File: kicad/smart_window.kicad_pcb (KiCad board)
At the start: 2 copper layers, 88 x 71.5 mm, 84 parts, among them J1 PROG, J10 LS2, J11 Vin, J12 LS3, J13 Vmot1, J14 Vmot3, J2 Vmot2, J3 DOOR1, J4 MOT2, J5 MOT1, J6 MOT3, J7 I2C, J8 DOOR2, J9 LS1, Q10 BC807-40_215, Q11 BC817-40_215, Q12 BC807-40_215, Q13 BC817-40_215, Q15 BC817-40_215, Q17 BC807-40_215, Q18 BC817-40_215, Q19 BC807-40_215, Q20 BC817-40_215, Q22 BC817-40_215, Q24 BC807-40_215, Q25 BC817-40_215, Q26 BC807-40_215, Q27 BC817-40_215, Q4 BC817-40_215, U1 ESP-12F, U3 LTV-817S, U4 LTV-817S, U5 LTV-817S, U6 LTV-817S, U7 LTV-817S, U8 LTV-817S

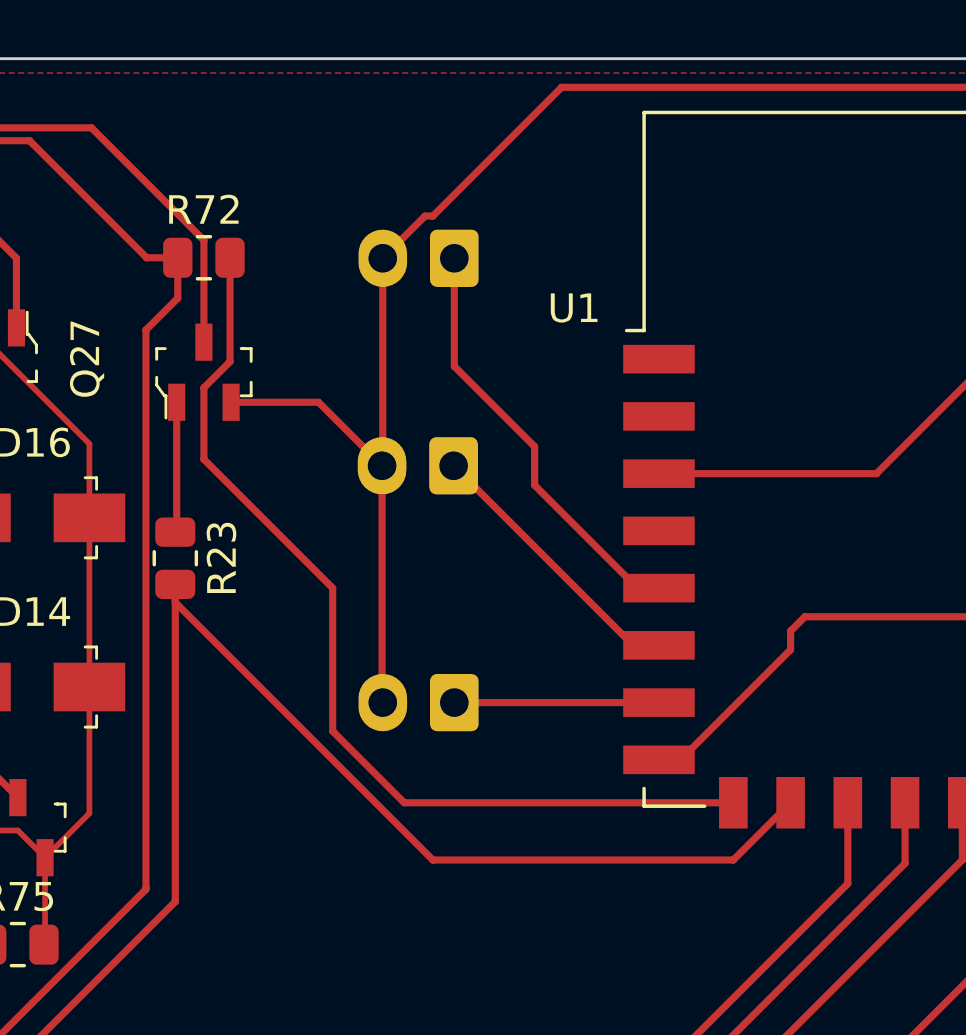
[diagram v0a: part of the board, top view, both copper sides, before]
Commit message: добавил фотосенсор
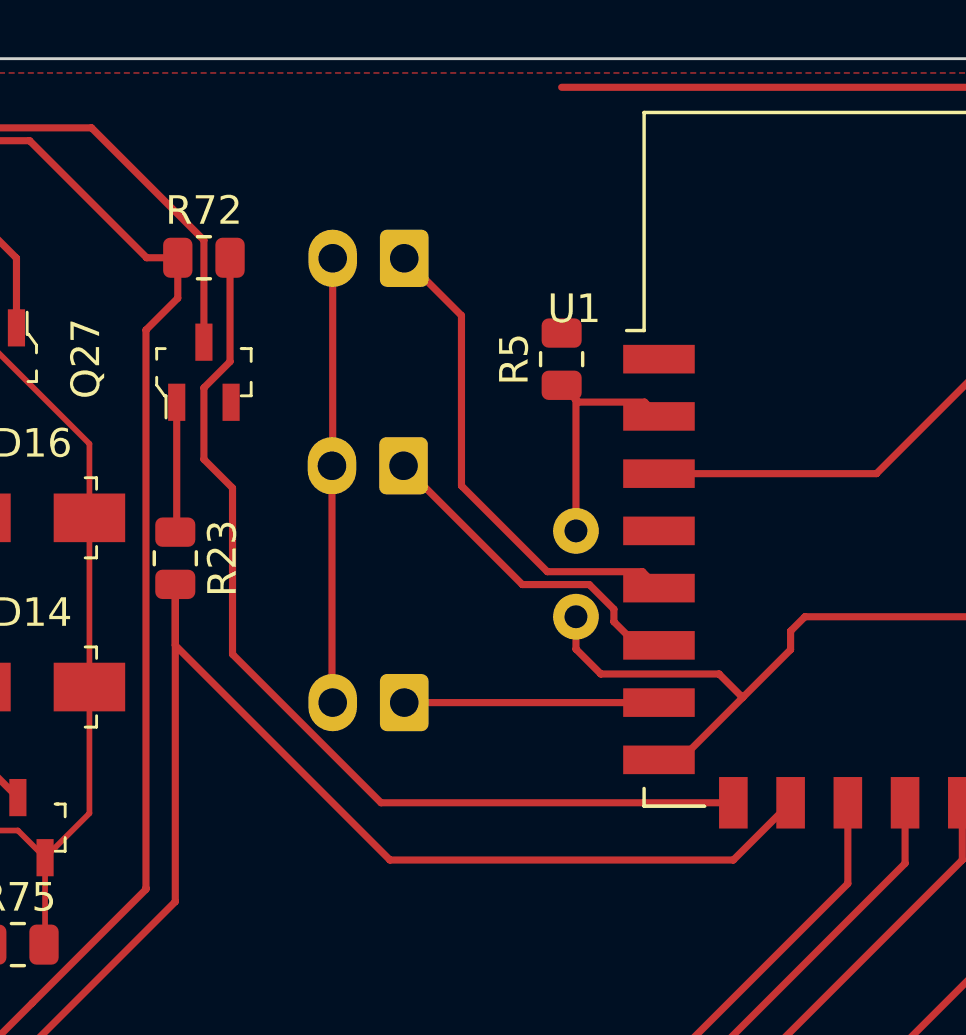
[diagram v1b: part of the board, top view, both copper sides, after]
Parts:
- added R4: A9050, OptoDevice:R_LDR_5.0x4.1mm_P3mm_Vertical, B.Cu at (131.5, 36.5)
- added R5: 500, Resistor_SMD:R_0805_2012Metric, F.Cu at (131.0, 27.5)
- moved J12 1.75 mm to (125.5, 39.5)
- moved J3 1.75 mm to (125.5, 24.0)
- moved J8 1.75 mm to (125.5, 31.2)
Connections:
- U1 pad 2: unconnected-(U1-Pad2) -> /LDR
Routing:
- net GND: track 240.0 -> 225.1 mm
- net /LDR: track 0.00 -> 9.15 mm
- net +3V3: track 41.3 -> 48.9 mm
- net /DOOR1: track 14.9 -> 17.9 mm
- net /DOOR2: track 9.77 -> 12.7 mm
- net /M3_LS: track 7.15 -> 8.90 mm
- net /M3_DIR: track 61.2 -> 62.1 mm

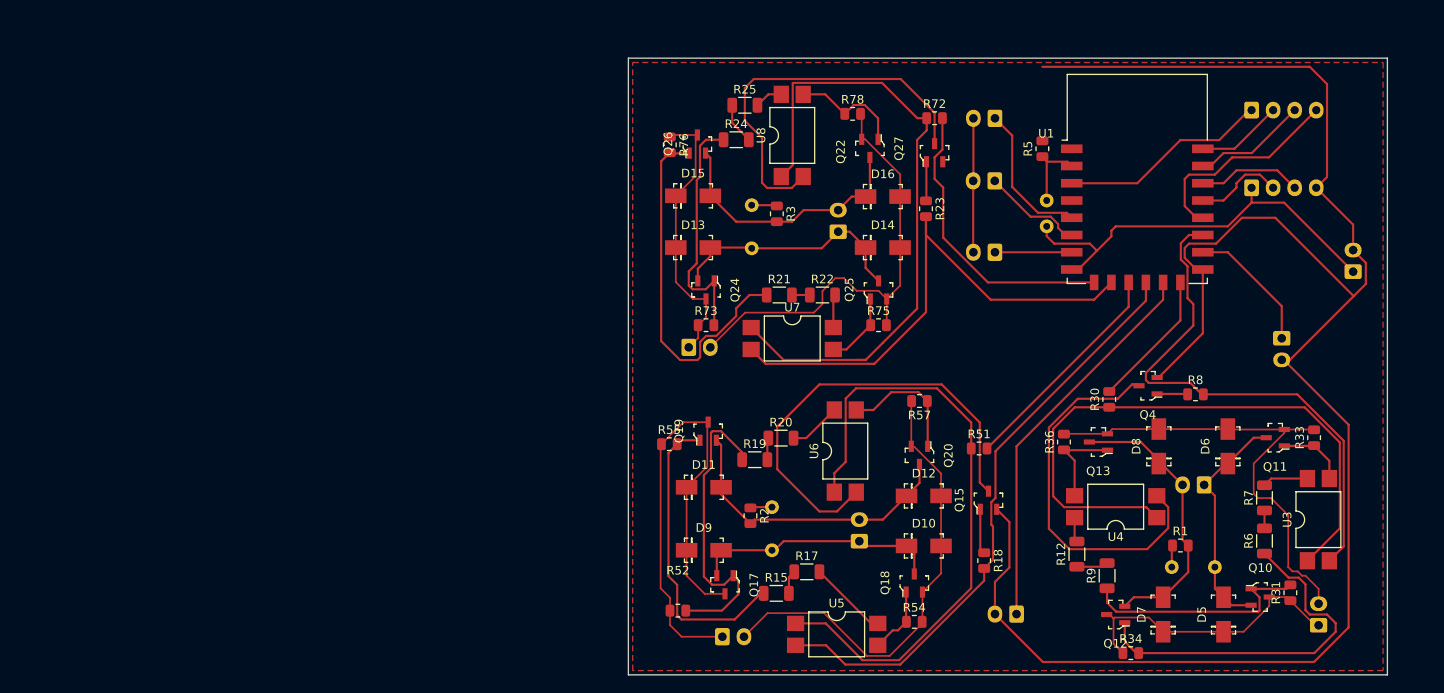
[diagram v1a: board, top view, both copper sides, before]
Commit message: добавлен DC-DC преобразователь для питания 3В от БП двигателя
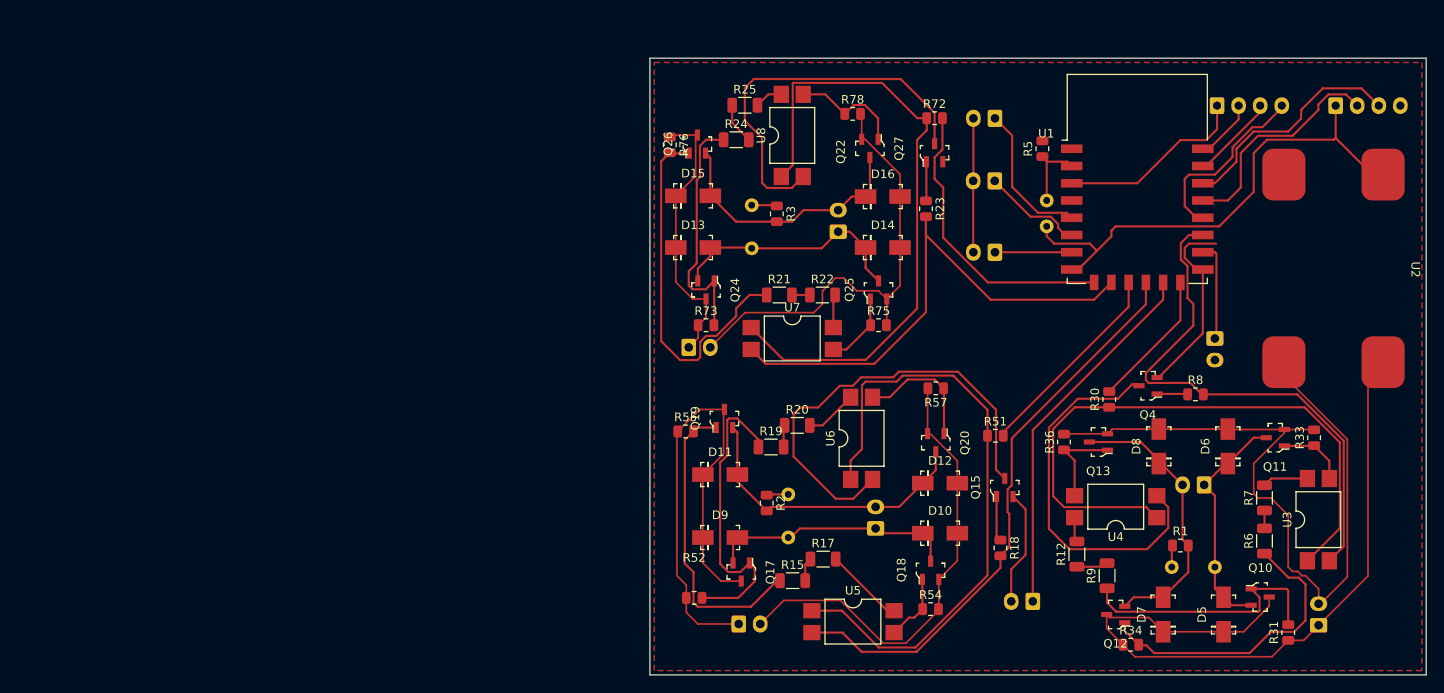
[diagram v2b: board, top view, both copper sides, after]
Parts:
- removed J11: Vin, Connector_JST:JST_XH_B2B-XH-A_1x02_P2.50mm_Vertical
- added U2: MP1584EN 3.3V, Power Modules:MP1584EN, F.Cu at (164.8, 41.5)
- moved J7 13.6 mm to (165.0, 22.5)
- moved J9 7.75 mm to (151.0, 49.5)
- moved R31 4.62 mm to (159.5, 83.6)
- moved J1 4.03 mm to (151.2, 22.5)
- moved Q19 2.40 mm to (94.1, 58.8)
- moved R51 2.40 mm to (125.5, 60.8)
- moved R55 2.40 mm to (89.6, 60.3)
- moved R57 2.40 mm to (118.6, 55.3)
- moved D10 2.40 mm to (119.1, 72.1)
- moved D11 2.40 mm to (93.6, 65.3)
- moved D12 2.40 mm to (119.1, 66.3)
- moved D9 2.40 mm to (93.6, 72.6)
- moved Q15 2.40 mm to (126.6, 66.8)
- moved Q17 2.40 mm to (96.1, 76.6)
- moved Q20 2.40 mm to (118.6, 61.6)
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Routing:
- net GND: track 225.1 -> 51.5 mm
- net /24V+1: track 33.6 -> 84.4 mm
- net /24V-1: track 55.5 -> 88.1 mm
- net /SDA: track 10.3 -> 26.2 mm
- net /SCL: track 12.1 -> 27.2 mm
- net +3V3: track 48.9 -> 56.6 mm
- net /h_bridge1/CCW: track 42.6 -> 34.9 mm
- net /M1_LS: track 15.5 -> 11.5 mm
- net /h_bridge1/CW: track 27.5 -> 31.1 mm
- net /ESP_RX: track 13.3 -> 9.99 mm
- net /ESP_GPIO0: track 24.4 -> 21.4 mm
- net /ESP_TX: track 10.0 -> 7.16 mm
- net /M2_LS: track 45.5 -> 43.2 mm
- net /M2_EN: track 26.1 -> 23.8 mm
- net /M2_DIR: track 69.3 -> 67.1 mm
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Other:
- board size 88 x 71.5 mm -> 90 x 71.5 mm

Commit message: версия с мостами на биполярных транзисторах
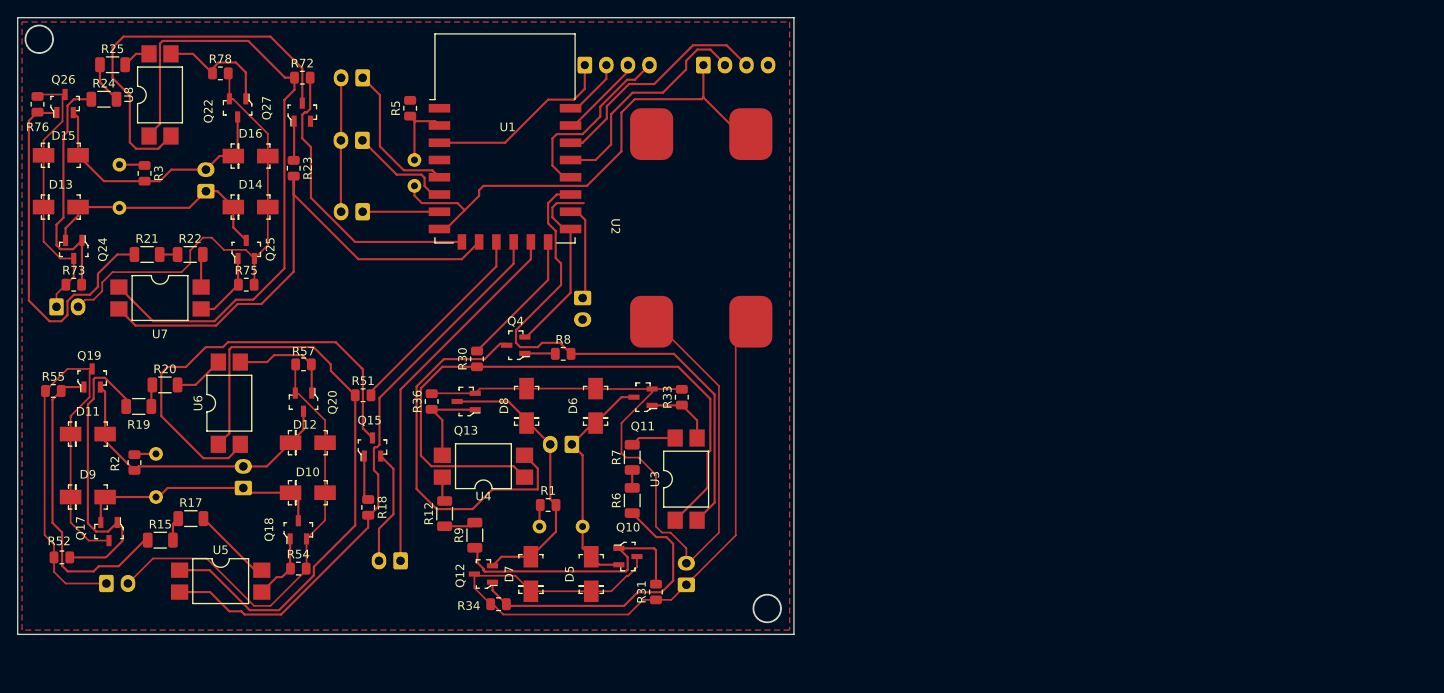
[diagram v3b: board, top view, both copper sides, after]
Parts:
- moved C2 73.5 mm to (77.7, 71.3)
- moved D10 73.5 mm to (45.8, 67.4)
- moved D11 73.5 mm to (20.3, 60.6)
- moved D12 73.5 mm to (45.8, 61.6)
- moved D13 73.5 mm to (17.2, 34.3)
- moved D15 73.5 mm to (17.2, 28.3)
- moved D5 73.5 mm to (78.7, 76.8)
- moved D6 73.5 mm to (79.2, 57.3)
- moved D7 73.5 mm to (71.7, 76.8)
- moved D8 73.5 mm to (71.2, 57.3)
- moved D9 73.5 mm to (20.3, 67.9)
- moved J1 73.5 mm to (77.9, 17.8)
- moved J13 73.5 mm to (89.7, 78.1)
- moved J14 73.5 mm to (16.7, 45.8)
- moved J5 73.5 mm to (76.4, 61.8)
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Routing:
- net Net-(Q20-Pad1): track 14.8 -> 12.4 mm
- net /h_bridge2/EN_IN: track 72.9 -> 71.0 mm
- net /24V-2: track 53.3 -> 51.9 mm
- net /h_bridge2/CW_O: track 52.8 -> 51.5 mm
- net /M1_DIR: track 62.1 -> 63.3 mm
- net Net-(Q27-Pad1): track 13.1 -> 14.0 mm
- net /M2_DIR: track 67.1 -> 67.9 mm
- net /h_bridge3/EN_IN: track 75.4 -> 74.7 mm
- net /h_bridge2/CCW: track 35.0 -> 35.7 mm
- net /h_bridge1/EN_IN: track 72.1 -> 72.7 mm
- net /24V-3: track 52.9 -> 53.5 mm
- net /h_bridge1/CW_O: track 44.4 -> 45.0 mm
- net /24V-1: track 88.1 -> 88.7 mm
- net /h_bridge3/CW_O: track 45.0 -> 45.6 mm
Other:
- outline, holes or cut-outs redrawn

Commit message: вариант с микросхемами a4950
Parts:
- removed D10, D11, D12, D13, D14, D15, D16, D5, D6, D7, D8, D9: SS14, digikey-footprints:DO-214AC
- removed J14: Vmot3, Connector_JST:JST_XH_B2B-XH-A_1x02_P2.50mm_Vertical
- removed J2: Vmot2, Connector_JST:JST_XH_B2B-XH-A_1x02_P2.50mm_Vertical
- removed Q10, Q12, Q17, Q19, Q24, Q26: BC807-40_215, digikey-footprints:SOT-23-3
- removed Q11, Q13, Q15, Q18, Q20, Q22, Q25, Q27, Q4: BC817-40_215, digikey-footprints:SOT-23-3
- removed R12, R15, R17, R19, R20, R21, R22, R24, R25, R6, R7, R9: 1.2k, Resistor_SMD:R_1206_3216Metric
- removed R18, R23, R8: 1.5k, Resistor_SMD:R_0805_2012Metric
- removed R30, R51, R72: 100, Resistor_SMD:R_0805_2012Metric
- removed R31, R33, R34, R36, R52, R54, R55, R57, R73, R75, R76, R78: 1k, Resistor_SMD:R_0805_2012Metric
- removed U6, U7, U8: LTV-817S, Package_DIP:SMDIP-4_W9.53mm
- added C1: 100µF, Capacitor_SMD:CP_Elec_10x10.5, F.Cu at (36.0, 31.5)
- added C5: 100µF, Capacitor_SMD:CP_Elec_10x10.5, F.Cu at (65.6, 59.3)
- added C6: 0.22µF, Capacitor_SMD:C_1206_3216Metric, F.Cu at (69.6, 50.8)
- C2, C4: value C -> 0.22µF; footprint Capacitor_THT:C_Radial_D10.0mm_H16.0mm_P5.00mm -> Capacitor_SMD:C_1206_3216Metric; moved to F.Cu
- C3: value C -> 100µF; footprint Capacitor_THT:C_Radial_D10.0mm_H16.0mm_P5.00mm -> Capacitor_SMD:CP_Elec_10x10.5; moved to F.Cu
- R1, R2, R3: value 50 -> 0.2; footprint Resistor_SMD:R_0805_2012Metric -> Resistor_SMD:R_1206_3216Metric
- U3, U4, U5: value LTV-817S -> A4950E; footprint Package_DIP:SMDIP-4_W9.53mm -> Package_SO:SOIC-8-1EP_3.9x4.9mm_P1.27mm_EP2.41x3.3mm
- moved R3 56.5 mm to (77.6, 55.3), turned to 180 degrees
- moved J6 51.0 mm to (74.9, 62.9), turned to 0 degrees
- moved U3 50.1 mm to (47.0, 39.5), turned to 180 degrees
- moved C2 49.3 mm to (45.5, 34.0)
- moved U5 48.9 mm to (75.6, 49.3), turned to -90 degrees
- moved J5 42.6 mm to (35.8, 49.0), turned to 0 degrees
- moved R1 42.6 mm to (41.0, 41.5), turned to 90 degrees
- moved J10 37.3 mm to (72.0, 41.2), turned to -90 degrees
- moved R2 29.8 mm to (54.5, 56.2), turned to 180 degrees
- moved C4 27.8 mm to (46.5, 50.8), turned to -90 degrees
- moved J13 20.6 mm to (88.8, 57.5), turned to 180 degrees
- moved U4 20.3 mm to (52.0, 49.8), turned to -90 degrees
- moved C3 17.7 mm to (44.0, 59.8), turned to 0 degrees
- moved J4 13.5 mm to (51.5, 63.8), turned to 0 degrees
- moved J9 3.78 mm to (79.0, 41.2)
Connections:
- C2 pad 1: /h_bridge1/ML -> GND
- C2 pad 2: Net-(C2-Pad2) -> /24V+
- C3 pad 1: /h_bridge2/ML -> GND
- C3 pad 2: Net-(C3-Pad2) -> /24V+
- C4 pad 1: /h_bridge3/ML -> GND
- C4 pad 2: Net-(C4-Pad2) -> /24V+
- J13 pad 1: /24V+1 -> /24V+
- J13 pad 2: /24V-1 -> GND
- J4 pad 1: /h_bridge2/ML -> Net-(J4-Pad1)
- J4 pad 2: /h_bridge2/MR -> Net-(J4-Pad2)
- J5 pad 1: /h_bridge1/ML -> Net-(J5-Pad1)
- J5 pad 2: /h_bridge1/MR -> Net-(J5-Pad2)
- J6 pad 1: /h_bridge3/ML -> Net-(J6-Pad1)
- J6 pad 2: /h_bridge3/MR -> Net-(J6-Pad2)
- R1 pad 1: Net-(C2-Pad2) -> GND
- R1 pad 2: /h_bridge1/MR -> Net-(U3-Pad7)
- R2 pad 1: Net-(C3-Pad2) -> GND
- R2 pad 2: /h_bridge2/MR -> Net-(U4-Pad7)
- R3 pad 1: Net-(C4-Pad2) -> GND
- R3 pad 2: /h_bridge3/MR -> Net-(U5-Pad7)
- U1 pad 10: /M3_DIR -> /M1_DIR
- U1 pad 14: /M1_EN -> /M3_DIR
- U1 pad 17: /M1_DIR -> /M3_EN
- U1 pad 4: unconnected-(U1-Pad4) -> /DOOR1
- U1 pad 5: /DOOR1 -> /DOOR2
- U1 pad 6: /DOOR2 -> /M1_EN
- U1 pad 9: /M3_EN -> unconnected-(U1-Pad9)
- U2 pad 3: /24V+1 -> /24V+
- U2 pad 4: /24V-1 -> GND
- U3 pad 1: /h_bridge1/EN_IN -> GND
- U3 pad 3: Net-(Q11-Pad1) -> /M1_EN
- U3 pad 4: Net-(R7-Pad2) -> +3V3
- U4 pad 1: /h_bridge1/EN_IN -> GND
- U4 pad 2: /h_bridge1/CW_O -> /M2_DIR
- U4 pad 3: Net-(Q13-Pad1) -> /M2_EN
- U4 pad 4: Net-(R12-Pad2) -> +3V3
- U5 pad 1: /h_bridge2/EN_IN -> GND
- U5 pad 2: /M2_DIR -> /M3_DIR
- U5 pad 3: Net-(Q18-Pad1) -> /M3_EN
- U5 pad 4: Net-(R17-Pad2) -> +3V3
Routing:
- net GND: track 51.5 -> 260.8 mm
- net /24V+: track 0.00 -> 152.9 mm
- net /24V-1: track 88.7 -> 0.00 mm
- net /24V+1: track 84.3 -> 0.00 mm
- net /h_bridge3/EN_IN: track 74.7 -> 0.00 mm
- net /h_bridge1/EN_IN: track 72.7 -> 0.00 mm
- net /h_bridge2/EN_IN: track 71.0 -> 0.00 mm
- net +3V3: track 56.6 -> 118.8 mm
- net /24V+2: track 58.7 -> 0.00 mm
- net /24V-3: track 53.5 -> 0.00 mm
- net /M3_DIR: track 62.3 -> 9.62 mm
- net /24V-2: track 51.9 -> 0.00 mm
- net /h_bridge2/CW_O: track 51.5 -> 0.00 mm
- net /M1_DIR: track 63.3 -> 17.1 mm
- net /M2_DIR: track 67.9 -> 21.8 mm
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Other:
- board size 90 x 71.5 mm -> 73.5 x 56 mm
